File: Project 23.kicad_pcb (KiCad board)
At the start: 2 copper layers, 62 x 42 mm, 48 parts, among them J11 SRX 1, J12 SRX 2, J13 SWD, J21 Batt, J61 USB_Micro, Q51 Si2315, SW11 UI_Btn, SW12 SW_SPST, U1 STM32F103C(8-B)Tx, U2 MCP73811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

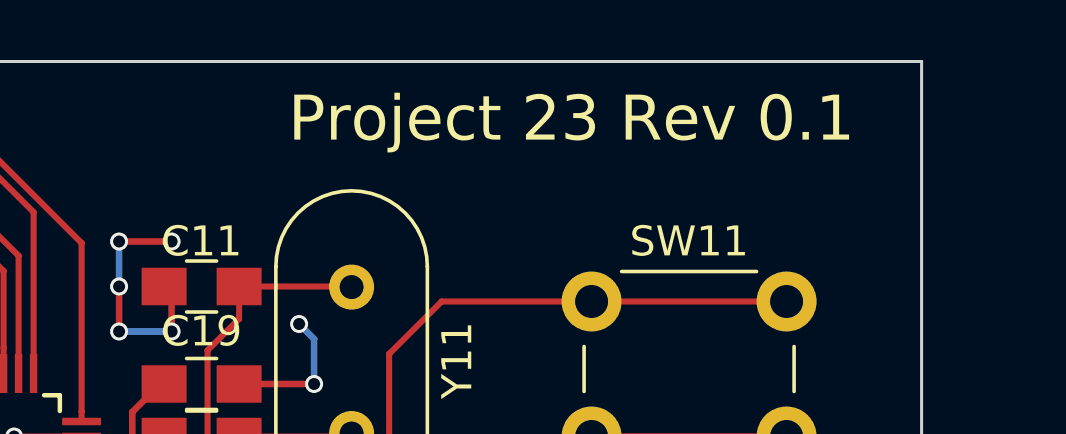
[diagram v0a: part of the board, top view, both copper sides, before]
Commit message: Fixed solder mask expansion ensured solder mask bridges between all pads of 0.5mm pitch LQFP-48 footprint. bumped revision to 0.4.
更正了阻焊开窗大小。 现在在0.5mm间距的LQFP-48封装的每个焊盘间都有阻焊桥。将版本提升至0.4。
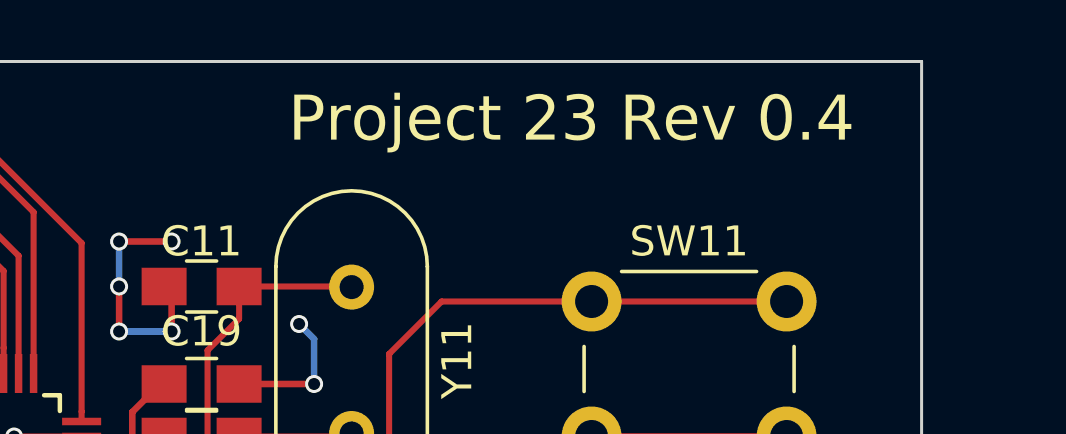
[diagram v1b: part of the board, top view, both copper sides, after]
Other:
- rule pad_to_mask_clearance: 0 -> 0.05
- board text added: "Project 23 Rev 0.4"
- board text removed: "Project 23 Rev 0.1"
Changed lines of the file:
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@@
     (links 135)
     (no_connects 0)
-    (area 49.949999 39.949999 112.050001 82.050001)
+    (area 48.775 39.949999 112.775 84.025)
     (thickness 1.6)
     (drawings 6)
@@
     (pad_size 1 1)
     (pad_drill 0.65)
-    (pad_to_mask_clearance 0)
+    (pad_to_mask_clearance 0.05)
     (aux_axis_origin 0 0)
     (visible_elements 7FFFFFFF)
     (pcbplotparams
       (layerselection 0x010f0_80000001)
-      (usegerberextensions false)
+      (usegerberextensions true)
       (excludeedgelayer false)
       (linewidth 0.100000)
@@
     (effects (font (size 1.5 1.5) (thickness 0.3)))
   )
-  (gr_text "Project 23 Rev 0.1\n" (at 100.33 41.91) (layer F.SilkS)
+  (gr_text "Project 23 Rev 0.4" (at 100.33 41.91) (layer F.SilkS)
     (effects (font (size 1.5 1.5) (thickness 0.3)))
   )

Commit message: Oled Connector fixed
Update to Version 0.4
Fixed oled connector
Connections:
- J11 pad 1: (no net) -> Net-(J11-Pad1)
- J11 pad 2: (no net) -> Net-(J11-Pad2)
- J13 pad 1: (no net) -> Net-(J13-Pad1)
- RN1 pad 1: (no net) -> Net-(RN1-Pad1)
- RN1 pad 8: (no net) -> Net-(RN1-Pad8)
- RN12 pad 1: (no net) -> Net-(RN12-Pad1)
- RN12 pad 3: (no net) -> Net-(RN12-Pad3)
- RN12 pad 6: (no net) -> Net-(RN12-Pad6)
- RN12 pad 8: (no net) -> Net-(RN12-Pad8)
- U1 pad 1: (no net) -> Net-(U1-Pad1)
- U1 pad 16: (no net) -> /MISO
- U1 pad 26: (no net) -> Net-(U1-Pad26)
- U1 pad 27: (no net) -> Net-(U1-Pad27)
- U1 pad 28: (no net) -> Net-(U1-Pad28)
- U1 pad 42: (no net) -> Net-(U1-Pad42)
- U1 pad 43: (no net) -> Net-(U1-Pad43)
- U1 pad 45: (no net) -> Net-(U1-Pad45)
- U1 pad 46: (no net) -> Net-(U1-Pad46)
- U1 pad 7: (no net) -> /Reset
- U3 pad 4: (no net) -> Net-(U3-Pad4)
- U4 pad 3: (no net) -> Net-(U4-Pad3)
- U5 pad 3: /OLED_CS -> /SCK
- U5 pad 4: /OLED_DC -> /MOSI
- U5 pad 6: /MOSI -> /OLED_DC
- U5 pad 7: /SCK -> /OLED_CS
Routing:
- net /OLED_CS: track 20.4 -> 10.2 mm, vias 2 -> 0
- net /SCK: track 9.97 -> 19.0 mm, vias 0 -> 2
- net /OLED_DC: track 21.6 -> 15.5 mm
- net /MOSI: track 10.6 -> 15.3 mm
- net /OLED_RES: track 20.4 -> 18.0 mm, vias 0 -> 2

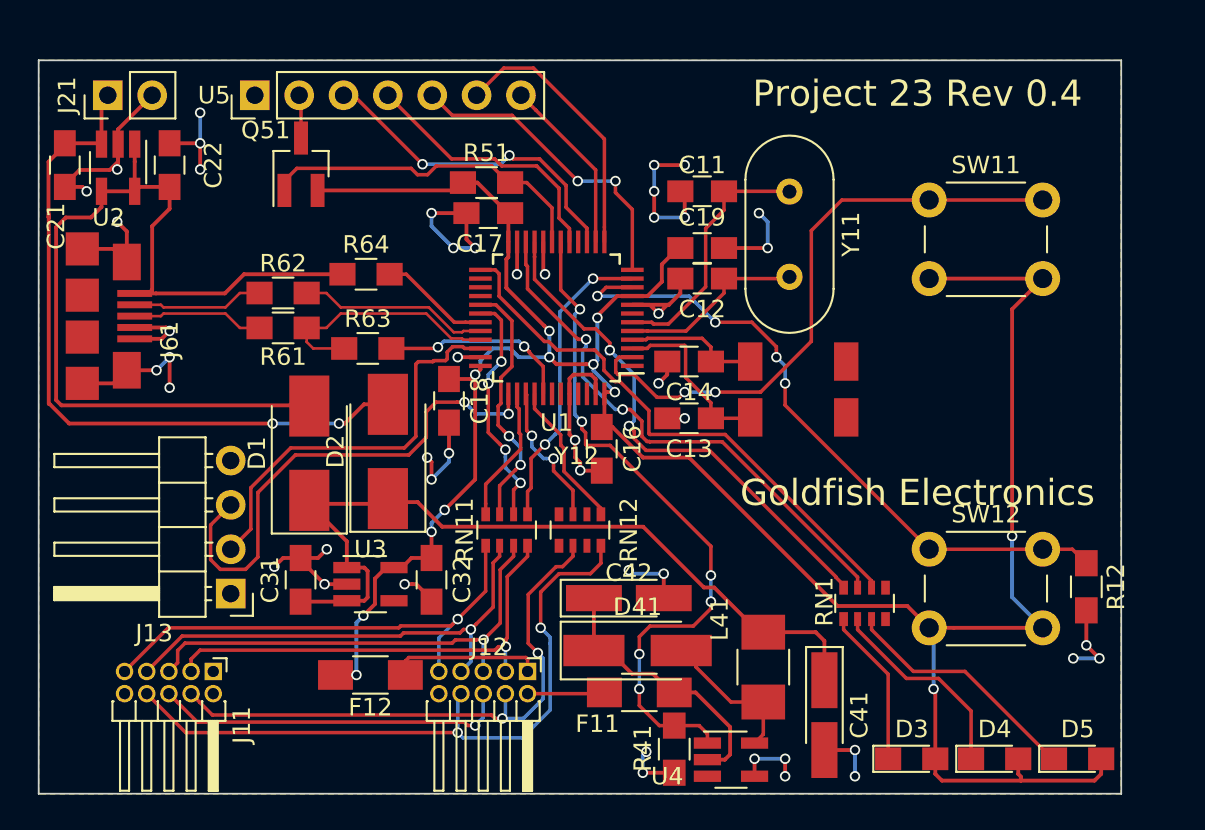
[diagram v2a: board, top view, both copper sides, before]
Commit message: Version 0.5
Removed 32k osc and added monting holes.
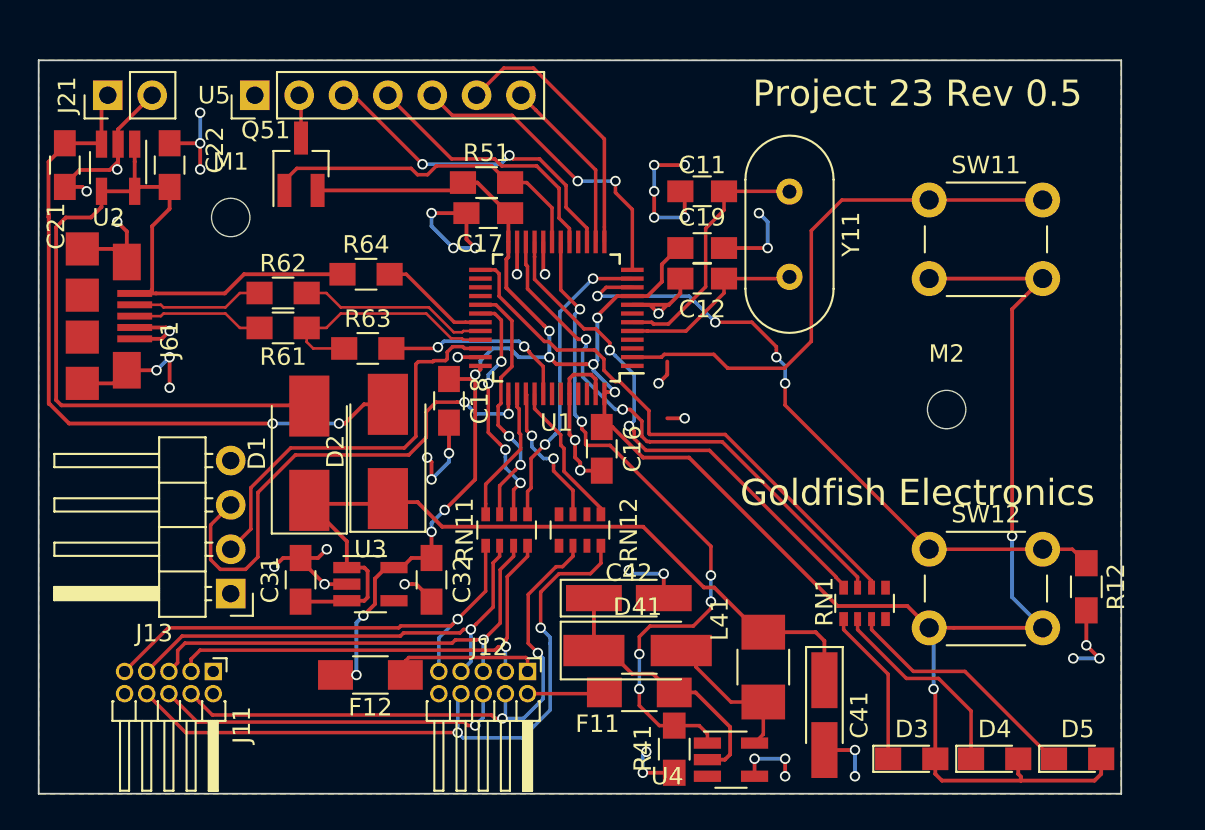
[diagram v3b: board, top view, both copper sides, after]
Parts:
- removed C13, C14: 20p, Capacitors_SMD:C_0805_HandSoldering
- removed Y12: 32khz, Project 23:ABS25
- added M1: Hole_M2, MountingHole:MountingHole_2.2mm_M2, F.Cu at (61.0, 49.0)
- added M2: Hole_M2, MountingHole:MountingHole_2.2mm_M2, F.Cu at (102.0, 60.0)
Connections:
- J11 pad 1: Net-(J11-Pad1) -> (no net)
- J11 pad 2: Net-(J11-Pad2) -> (no net)
- J13 pad 1: Net-(J13-Pad1) -> (no net)
- RN1 pad 1: Net-(RN1-Pad1) -> (no net)
- RN1 pad 8: Net-(RN1-Pad8) -> (no net)
- RN12 pad 1: Net-(RN12-Pad1) -> (no net)
- RN12 pad 3: Net-(RN12-Pad3) -> (no net)
- RN12 pad 6: Net-(RN12-Pad6) -> (no net)
- RN12 pad 8: Net-(RN12-Pad8) -> (no net)
- U1 pad 1: Net-(U1-Pad1) -> (no net)
- U1 pad 16: /MISO -> (no net)
- U1 pad 26: Net-(U1-Pad26) -> (no net)
- U1 pad 27: Net-(U1-Pad27) -> (no net)
- U1 pad 28: Net-(U1-Pad28) -> (no net)
- U1 pad 3: Net-(C13-Pad1) -> (no net)
- U1 pad 4: Net-(C14-Pad1) -> (no net)
- U1 pad 42: Net-(U1-Pad42) -> (no net)
- U1 pad 43: Net-(U1-Pad43) -> (no net)
- U1 pad 45: Net-(U1-Pad45) -> (no net)
- U1 pad 46: Net-(U1-Pad46) -> (no net)
- U1 pad 7: /Reset -> (no net)
- U3 pad 4: Net-(U3-Pad4) -> (no net)
- U4 pad 3: Net-(U4-Pad3) -> (no net)
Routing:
- net Net-(C13-Pad1): track 10.1 -> 0.00 mm
- net Net-(C14-Pad1): track 7.82 -> 0.00 mm
- net /UI_Btn: track 35.1 -> 31.6 mm, vias 2 -> 0
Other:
- board text added: "Project 23 Rev 0.5"
- board text removed: "Project 23 Rev 0.4"

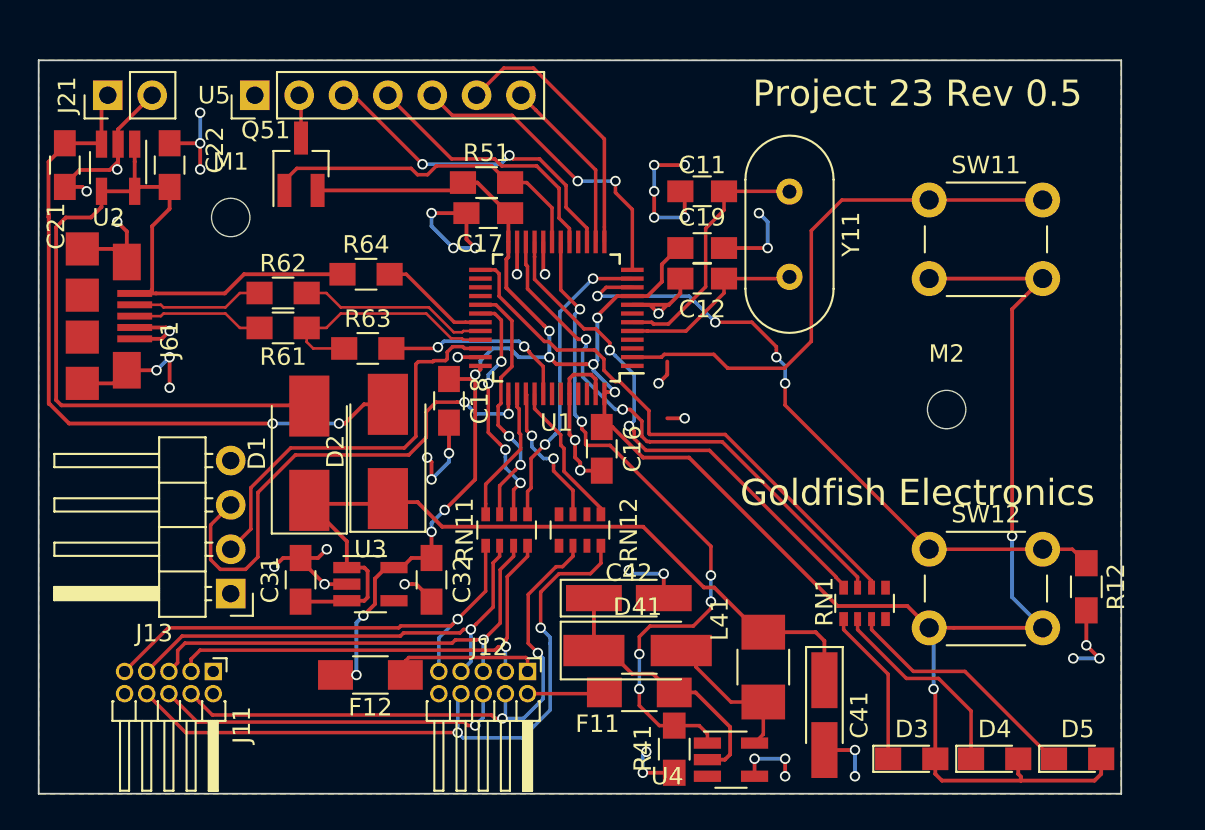
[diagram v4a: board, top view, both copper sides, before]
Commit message: Updated footprints to Kicad 5.0.0 librarys
Updated footprints to Kicad 5.0.0 Libraries. Switched C41 and C42 to EIA 3528-21 and EIA 6032-28 respectively.
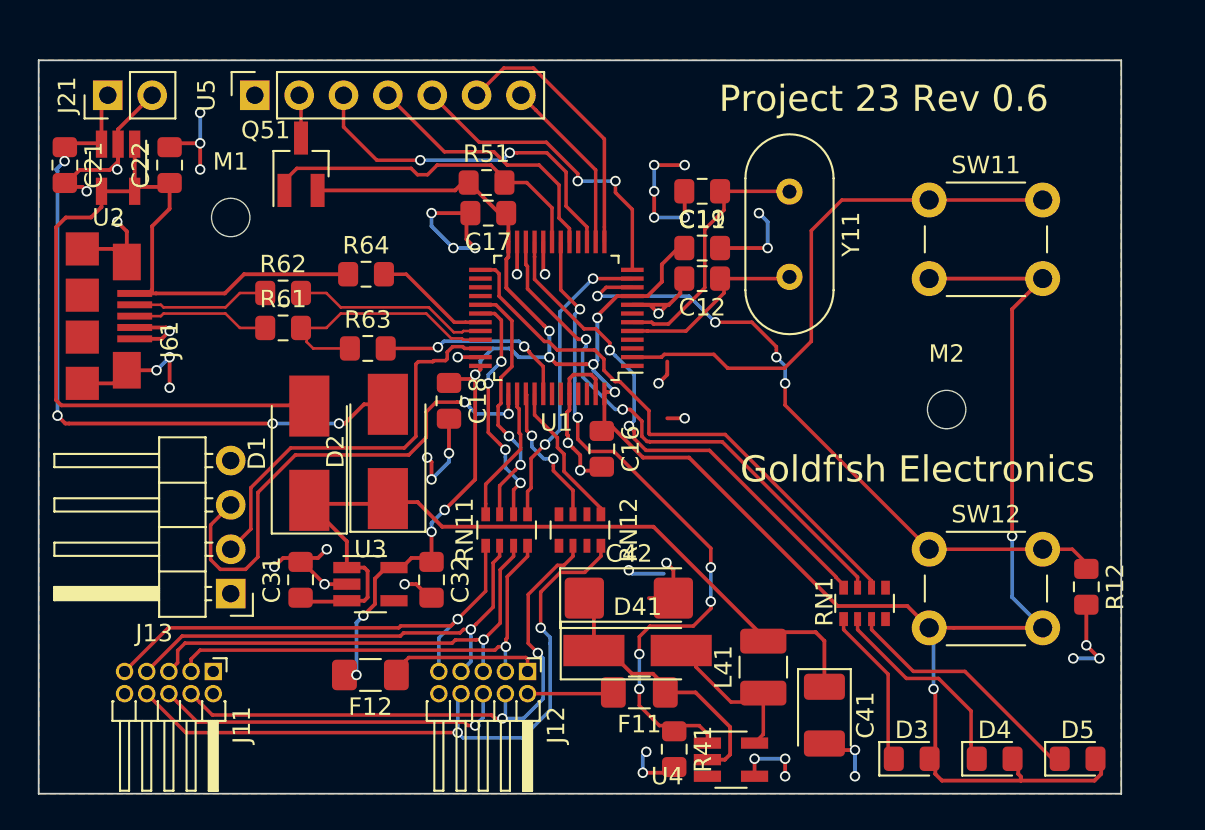
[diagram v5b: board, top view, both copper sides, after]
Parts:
- C11, C12, C16, C17, C18, C19, C21, C22, C31, C32: footprint Capacitors_SMD:C_0805_HandSoldering -> Capacitor_SMD:C_0805_2012Metric_Pad1.15x1.40mm_HandSolder
- C41: footprint Capacitors_Tantalum_SMD:CP_Tantalum_Case-A_EIA-3216-18_Hand -> Capacitor_Tantalum_SMD:CP_EIA-3528-21_Kemet-B_Pad1.50x2.35mm_HandSolder
- C42: footprint Capacitors_Tantalum_SMD:CP_Tantalum_Case-A_EIA-3216-18_Hand -> Capacitor_Tantalum_SMD:CP_EIA-6032-28_Kemet-C_Pad2.25x2.35mm_HandSolder
- D1, D2: footprint Diodes_SMD:D_SMB_Handsoldering -> Diode_SMD:D_SMB_Handsoldering
- D3, D4, D5: footprint LEDs:LED_0805_HandSoldering -> LED_SMD:LED_0805_2012Metric_Pad1.15x1.40mm_HandSolder
- D41: footprint Diodes_SMD:D_SMA_Handsoldering -> Diode_SMD:D_SMA_Handsoldering
- F11, F12: footprint Resistors_SMD:R_1206_HandSoldering -> Fuse:Fuse_1206_3216Metric_Pad1.42x1.75mm_HandSolder
- J11, J12: footprint Pin_Headers:Pin_Header_Angled_2x05_Pitch1.27mm -> Connector_PinHeader_1.27mm:PinHeader_2x05_P1.27mm_Horizontal
- J13: footprint Pin_Headers:Pin_Header_Angled_1x04_Pitch2.54mm -> Connector_PinHeader_2.54mm:PinHeader_1x04_P2.54mm_Horizontal
- J21: footprint Pin_Headers:Pin_Header_Straight_1x02_Pitch2.54mm -> Connector_PinHeader_2.54mm:PinHeader_1x02_P2.54mm_Vertical
- L41: footprint Resistors_SMD:R_1210_HandSoldering -> Inductor_SMD:L_1210_3225Metric_Pad1.42x2.65mm_HandSolder
- Q51: footprint TO_SOT_Packages_SMD:SOT-23_Handsoldering -> Package_TO_SOT_SMD:SOT-23_Handsoldering
- R12, R41, R51, R61, R62, R63, R64: footprint Resistors_SMD:R_0805_HandSoldering -> Resistor_SMD:R_0805_2012Metric_Pad1.15x1.40mm_HandSolder
- RN1, RN11, RN12: footprint Resistors_SMD:R_Array_Convex_4x0603 -> Resistor_SMD:R_Array_Convex_4x0603
- SW11: footprint Buttons_Switches_ThroughHole:SW_PUSH_6mm -> Button_Switch_THT:SW_PUSH_6mm_H5mm
- SW12: value SW_SPST -> PWR_BTN; footprint Buttons_Switches_ThroughHole:SW_PUSH_6mm -> Button_Switch_THT:SW_PUSH_6mm_H5mm
- U1: value STM32F103C(8-B)Tx -> STM32F103C8T7; footprint Housings_QFP:LQFP-48_7x7mm_Pitch0.5mm -> Package_QFP:LQFP-48_7x7mm_P0.5mm
- U2, U3, U4: footprint TO_SOT_Packages_SMD:SOT-23-5_HandSoldering -> Package_TO_SOT_SMD:SOT-23-5_HandSoldering
- U5: footprint Pin_Headers:Pin_Header_Straight_1x07_Pitch2.54mm -> Connector_PinSocket_2.54mm:PinSocket_1x07_P2.54mm_Vertical
- Y11: footprint Crystals:Crystal_HC49-U_Vertical -> Crystal:Crystal_HC49-4H_Vertical
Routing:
- net /SCK: track 19.0 -> 21.1 mm
- net GND: track 109.8 -> 110.7 mm
- net +BATT: track 40.9 -> 40.4 mm, vias 2 -> 4
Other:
- board text added: "Project 23 Rev 0.6"
- board text removed: "Project 23 Rev 0.5"

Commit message: Generated up to date gerber
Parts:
- renumbered M1 to 1
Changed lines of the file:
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@@
     (38 B.Mask user)
     (39 F.Mask user)
-    (40 Dwgs.User user)
-    (41 Cmts.User user)
-    (42 Eco1.User user)
+    (40 Dwgs.User user hide)
+    (41 Cmts.User user hide)
+    (42 Eco1.User user hide)
     (43 Eco2.User user)
     (44 Edge.Cuts user)
     (45 Margin user)
-    (46 B.CrtYd user)
-    (47 F.CrtYd user)
-    (48 B.Fab user)
-    (49 F.Fab user)
+    (46 B.CrtYd user hide)
+    (47 F.CrtYd user hide)
+    (48 B.Fab user hide)
+    (49 F.Fab user hide)
   )
   (setup
@@
     (visible_elements 7FFFFFFF)
     (pcbplotparams
-      (layerselection 0x01020_7ffffffe)
+      (layerselection 0x010f0_ffffffff)
       (usegerberextensions true)
       (usegerberattributes false)
@@
       (padsonsilk false)
       (subtractmaskfromsilk false)
-      (outputformat 4)
+      (outputformat 1)
       (mirror false)
       (drillshape 0)
       (scaleselection 1)
-      (outputdirectory ""))
+      (outputdirectory "Gerber/"))
   )
   (net 0 "")
@@
       (net 6 VBUS))
   )
-  (module MountingHole:MountingHole_2.2mm_M2 (layer F.Cu)
+  (module MountingHole:MountingHole_2.2mm_M2 locked (layer F.Cu)
     (at 61 49)
     (descr "Mounting Hole 2.2mm, no annular, M2")
     (tags "mounting hole 2.2mm no annular m2")
     (attr virtual)
-    (fp_text reference M1 (at 0 -3.2) (layer F.SilkS)
+    (fp_text reference 1 (at 0 -3.2) (layer F.SilkS)
       (effects (font (size 1 1) (thickness 0.15)))
     )
@@
     (pad 1 np_thru_hole circle (at 0 0) (size 2.2 2.2) (drill 2.2) (layers *.Cu *.Mask))
   )
-  (module MountingHole:MountingHole_2.2mm_M2 (layer F.Cu)
+  (module MountingHole:MountingHole_2.2mm_M2 locked (layer F.Cu)
     (at 102 60)
     (descr "Mounting Hole 2.2mm, no annular, M2")
@@
     (tags "capacitor tantalum")
     (attr smd)
-    (fp_text reference C42 (at 0 -2.55) (layer F.SilkS)
+    (fp_text reference C42 (at 0.0962 0.0152) (layer F.SilkS)
       (effects (font (size 1 1) (thickness 0.15)))
     )
@@
     (tags "capacitor handsolder")
     (attr smd)
-    (fp_text reference C11 (at 0 -1.65 180) (layer F.SilkS)
+    (fp_text reference C11 (at 0.0144 1.8308 180) (layer F.SilkS)
       (effects (font (size 1 1) (thickness 0.15)))
     )
@@
     (tags "capacitor handsolder")
     (attr smd)
-    (fp_text reference C17 (at 0 -1.65 180) (layer F.SilkS)
+    (fp_text reference C17 (at 0.9724 -1.6944 180) (layer F.SilkS)
       (effects (font (size 1 1) (thickness 0.15)))
     )
@@
     (tags "capacitor handsolder")
     (attr smd)
-    (fp_text reference C21 (at 0 -1.65 270) (layer F.SilkS)
+    (fp_text reference C21 (at 2.8442 -0.0366) (layer F.SilkS)
       (effects (font (size 1 1) (thickness 0.15)))
     )
@@
     (tags "capacitor handsolder")
     (attr smd)
-    (fp_text reference C22 (at 0 -1.65 90) (layer F.SilkS)
+    (fp_text reference C22 (at 0.0514 1.8344 90) (layer F.SilkS)
       (effects (font (size 1 1) (thickness 0.15)))
     )
@@
     (tags "capacitor handsolder")
     (attr smd)
-    (fp_text reference C32 (at 0 -1.65 270) (layer F.SilkS)
+    (fp_text reference C32 (at 0.9636 -1.6934 270) (layer F.SilkS)
       (effects (font (size 1 1) (thickness 0.15)))
     )
@@
     (tags "Diode SMA (DO-214AC) Handsoldering")
     (attr smd)
-    (fp_text reference D41 (at 0 -2.5) (layer F.SilkS)
+    (fp_text reference D41 (at -3.655 2.3746) (layer F.SilkS)
       (effects (font (size 1 1) (thickness 0.15)))
     )
@@
     (tags "resistor handsolder")
     (attr smd)
-    (fp_text reference R41 (at 0 -1.65 270) (layer F.SilkS)
+    (fp_text reference R41 (at 0.3568 1.6148 270) (layer F.SilkS)
       (effects (font (size 1 1) (thickness 0.15)))
     )
@@
     (tags "SOT-23-5 hand-soldering")
     (attr smd)
-    (fp_text reference U2 (at 2.85 0.55) (layer F.SilkS)
+    (fp_text reference U2 (at 2.7704 -0.0346) (layer F.SilkS)
       (effects (font (size 1 1) (thickness 0.15)))
     )
@@
     (tags "SOT-23-5 hand-soldering")
     (attr smd)
-    (fp_text reference U4 (at -3.65 0.95) (layer F.SilkS)
-      (effects (font (size 1 1) (thickness 0.15)))
-    )
+    (fp_text reference U4 (at 2.9584 -0.04 90) (layer F.SilkS)
+      (effects (font (size 1 1) (thickness 0.15)))
+    )
